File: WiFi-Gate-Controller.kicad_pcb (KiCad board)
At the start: 2 copper layers, 66 x 51.5 mm, 91 parts, among them J1 Screw_Terminal_01x10, J2 USB_B_Micro, J3 Cortex Debug, SW1 Reset, U1 BTS3800SL, U10 SAMD21G18-M, U11 74LVC2G14, U12 74LVC2G14, U2 LMZ21700, U3 BTS3800SL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

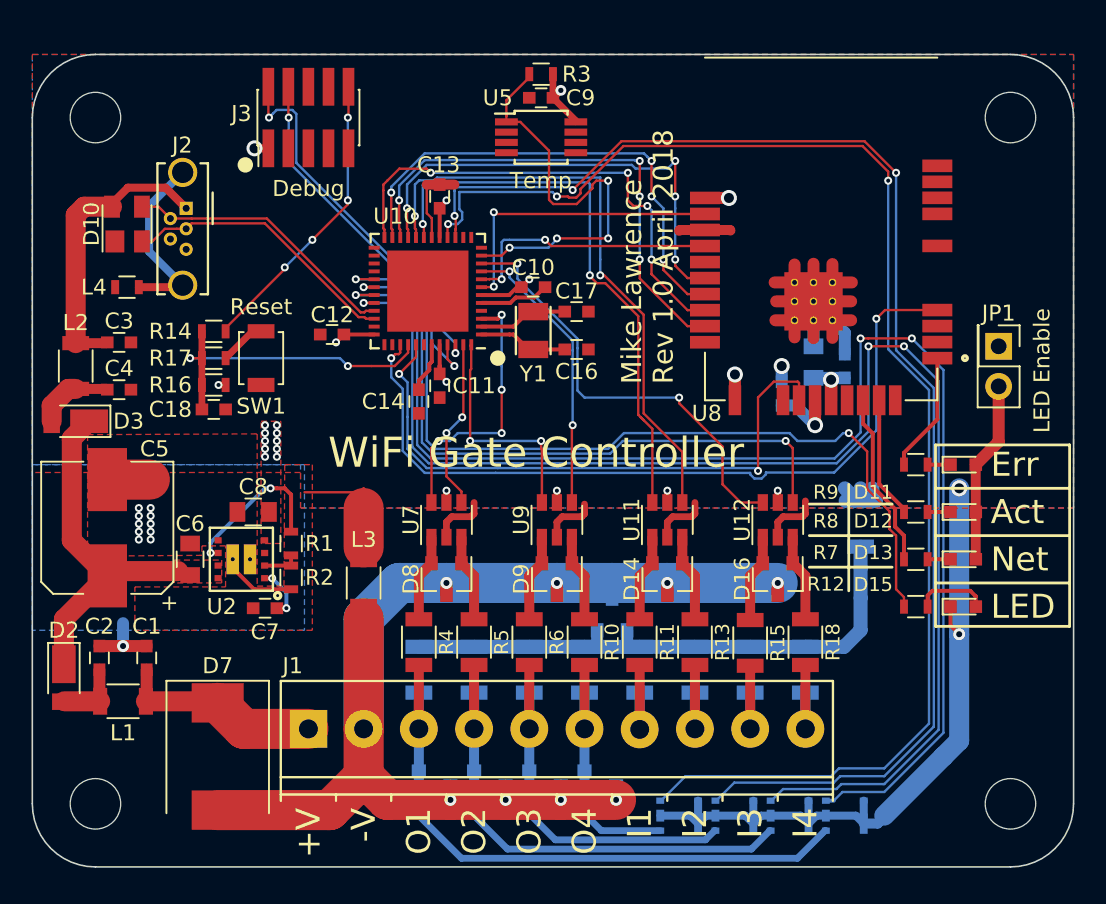
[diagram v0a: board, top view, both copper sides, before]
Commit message: Update to KiCad 5.1 libraries.
Also updated custom libraries.
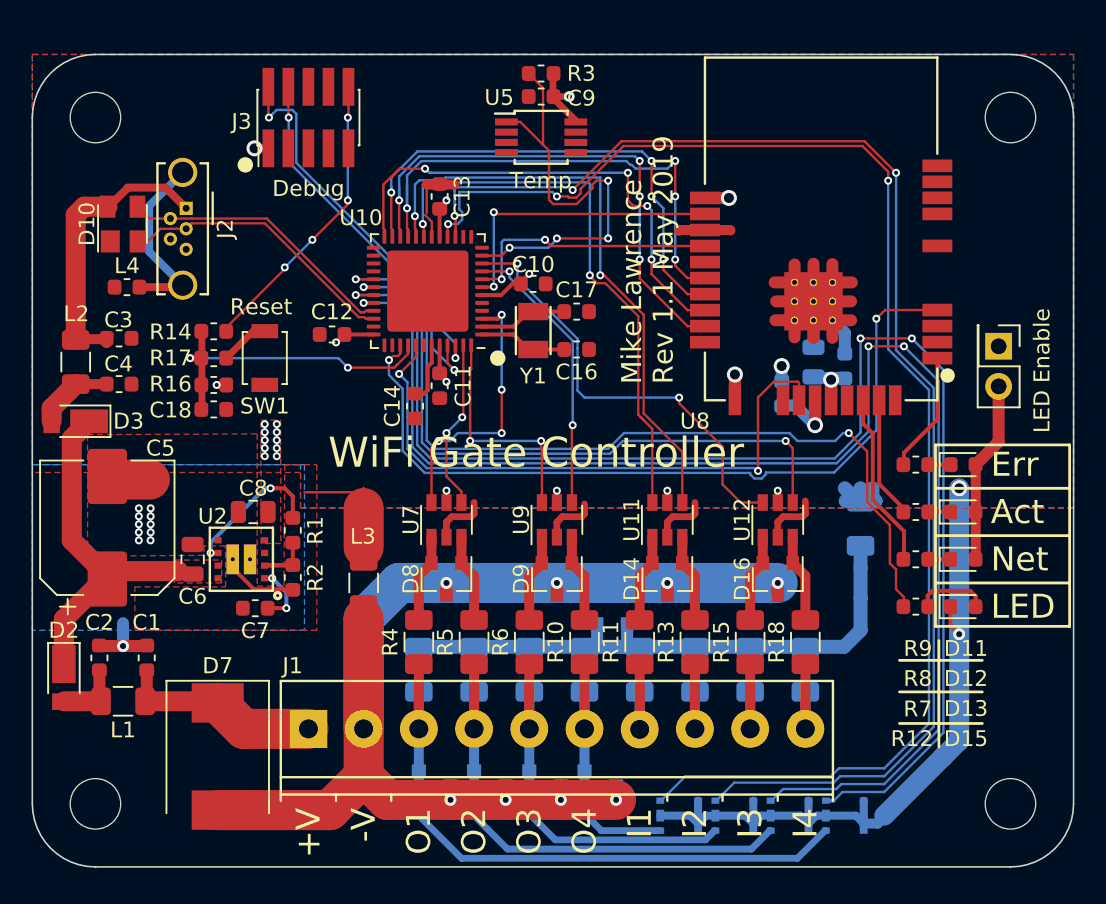
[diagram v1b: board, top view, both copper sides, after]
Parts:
- C1, C10, C11, C12, C13, C14, C15, C16, C17, C18, C2, C20, C3, C4, C7, C9: footprint Capacitors_SMD:C_0603 -> Capacitor_SMD:C_0603_1608Metric
- C19, C6, C8: footprint Capacitors_SMD:C_0805 -> Capacitor_SMD:C_0805_2012Metric
- C5: footprint Capacitors_SMD:CP_Elec_8x10 -> Capacitor_SMD:CP_Elec_8x10
- D1, D14, D16, D17, D4, D5, D6, D8, D9: footprint TO_SOT_Packages_SMD:SOT-23 -> Package_TO_SOT_SMD:SOT-23
- D10: footprint TO_SOT_Packages_SMD:SOT-143 -> Package_TO_SOT_SMD:SOT-143
- D11, D12, D13, D15: footprint LEDs:LED_0603 -> LED_SMD:LED_0603_1608Metric
- D2, D3: footprint Diodes_SMD:D_PowerDI-123 -> Diode_SMD:D_PowerDI-123
- D7: footprint Diodes_SMD:D_SMC -> Diode_SMD:D_SMC
- J2: footprint Connectors_USB:USB_Micro-B_Wuerth-614105150721_Vertical_CircularHoles -> Connector_USB:USB_Micro-B_Wuerth_614105150721_Vertical_CircularHoles
- J3: footprint Pin_Headers:Pin_Header_Straight_2x05_Pitch1.27mm_SMD -> Connector_PinHeader_1.27mm:PinHeader_2x05_P1.27mm_Vertical_SMD
- JP1: footprint Pin_Headers:Pin_Header_Straight_2x01_Pitch2.54mm -> Connector_PinHeader_2.54mm:PinHeader_2x01_P2.54mm_Vertical
- L1, L2, L3, L5: footprint Inductors_SMD:L_1206 -> Inductor_SMD:L_1206_3216Metric
- L4: footprint Inductors_SMD:L_0603 -> Inductor_SMD:L_0603_1608Metric
- R1, R12, R14, R16, R17, R2, R3, R7, R8, R9: footprint Resistors_SMD:R_0603 -> Resistor_SMD:R_0603_1608Metric
- R10, R11, R13, R15, R18, R20, R21, R22, R23, R24, R25, R26, R27, R4, R5, R6: footprint Resistors_SMD:R_1206 -> Resistor_SMD:R_1206_3216Metric
- SW1: footprint Buttons_Switches_SMD:SW_SPST_B3U-1000P -> Button_Switch_SMD:SW_SPST_B3U-1000P
- U1, U3, U4, U6: footprint infineon-ml:SCT595 -> Package_TO_SOT_SMD-ML:Infineon_PG-SCT595-5-1
- U10: footprint Housings_DFN_QFN:QFN-48-1EP_7x7mm_Pitch0.5mm -> Package_DFN_QFN:QFN-48-1EP_7x7mm_P0.5mm_EP5.15x5.15mm
- U11, U12, U7, U9: footprint TO_SOT_Packages_SMD:SOT-23-6 -> Package_TO_SOT_SMD:SOT-23-6
- U2: footprint ti-ml:SIL0008E -> Converter_DCDC-ML:Converter_DCDC_Texas-SIL0008E
- U5: footprint Housings_SSOP:MSOP-8_3x3mm_Pitch0.65mm -> Package_SO:MSOP-8_3x3mm_P0.65mm
- U8: footprint atmel-ml:ATWINC1500-MR210XB -> RF_Module-ML:Microchip_ATWINC1500-MR210UB
- Y1: footprint abracon-ml:ABS07 -> Crystal-ML:Crystal_SMD_Abracon_ABS07-2Pin_3.2x1.5mm
- moved R1 0.84 mm to (42.5, 61.7)
- moved C7 0.62 mm to (40.1, 66.6)
- moved D17 0.38 mm to (62.8, 66.6)
- moved C14 0.38 mm to (50.3, 53.8)
- moved C4 0.35 mm to (31.5, 52.4)
- moved D10 0.29 mm to (31.7, 42.2)
- moved C3 0.25 mm to (31.5, 49.5)
- moved L2 0.25 mm to (28.8, 51.0)
- moved SW1 0.23 mm to (40.7, 50.7)
- moved C10 0.21 mm to (57.8, 46.0)
- moved C6 0.16 mm to (36.2, 63.5)
- moved R2 0.11 mm to (42.5, 64.7)
- moved C9 0.08 mm to (58.2, 34.2)
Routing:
- net GND: track 131.4 -> 126.9 mm
- net Net-(R1-Pad2): track 2.32 -> 4.89 mm
- net /WINC_MOSI: track 30.0 -> 32.1 mm
- net /WINC_SCK: track 32.1 -> 33.6 mm
- net /A5: track 27.0 -> 28.4 mm
- net /SWDIO: track 23.9 -> 25.0 mm
- net GNDPWR: track 79.3 -> 78.3 mm
- net Net-(D17-Pad1): track 36.3 -> 37.2 mm
- net /~WINC_SS: track 31.3 -> 32.1 mm
- net /~RESET~: track 20.6 -> 21.3 mm
- net Net-(C14-Pad2): track 3.19 -> 3.84 mm
- net /~WINC_RST: track 50.7 -> 51.3 mm
- net Net-(C7-Pad1): track 3.42 -> 4.00 mm
- net VCC: track 42.6 -> 43.1 mm
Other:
- board text added: "Rev 1.1 May 2019"
- board text removed: "Rev 1.0 April 2018"
